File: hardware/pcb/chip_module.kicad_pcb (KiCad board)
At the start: 4 copper layers, 70 x 50 mm, 17 parts, among them J1 Samtec LSHM-130, U1 ADG732BCPZ, U2 ADG732BCPZ, U3 ADA4530-1, U4 74LVC1G04, U5 QSSC_Chip

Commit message: pcb: chip module copper-plane foundation + power-rail test points
route_qssc_pcb.py is board-agnostic (QSSC_PCB_PATH env override), so run the
copper-plane pass on the swappable chip module: 4 zones (In1.Cu GND, In2.Cu
+3V3, F.Cu/B.Cu GND floods) + 30 GND stitching vias -> the 64 analog detector
lines and the TIA sit over a continuous ground reference.

The +3V3 pour was an isolated-copper fill (all +3V3 pads are SMD, no plated
hole ties the In2.Cu plane to the rail). Each module PWR_FLAG now carries a
real thru-hole TestPoint_Loop footprint, giving 4 probeable power-rail points
(+3V3/+5V/+7V_EMIT/GND) on the left edge; the plated +3V3 pad stitches the
plane (same mechanism by which the main board's thru-hole RESET button keeps
its +3V3 plane non-isolated).

kicad-cli pcb drc: 0 violations / 0 unconnected / 0 footprint errors (was 1
isolated_copper warning). ERC unchanged (0 errors / 26 warnings). pytest 122
passed, 2 skipped; ruff clean.

Note recorded in HARDWARE_DESIGN.md §15A: TPS61023 (max output 5.5V) cannot
produce the +7V_EMIT rail — use a >=7V part (e.g. TPS61040) once the emitter
driver topology is fixed. *.kicad_prl gitignored (KiCad project-local file).

Co-Authored-By: Claude <noreply@anthropic.com>
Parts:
- added #FLG1: PWR_FLAG, TestPoint_Loop_D1.80mm_Drill1.0mm_Beaded, F.Cu at (6.00, 4.00)
- added #FLG2: PWR_FLAG, TestPoint_Loop_D1.80mm_Drill1.0mm_Beaded, F.Cu at (6.00, 9.00)
- added #FLG3: PWR_FLAG, TestPoint_Loop_D1.80mm_Drill1.0mm_Beaded, F.Cu at (6.00, 14.0)
- added #FLG4: PWR_FLAG, TestPoint_Loop_D1.80mm_Drill1.0mm_Beaded, F.Cu at (6.00, 19.0)
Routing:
- net GND: vias 0 -> 30
- added copper zone on In2.Cu, net +3V3
- added copper zone on B.Cu, net GND
- added copper zone on F.Cu, net GND
- added copper zone on In1.Cu, net GND

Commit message: chip module: place discrete MOSFET emitter crossbar (+5V), eliminate +7V_EMIT
Emitter driver for the 8x8 CQD matrix is now placed on the swappable chip
module as the simplest-functional topology (29 parts, no boost / no DAC /
no TLC5955): 2x 74HCT240 inverting level-shifters (3.3V FPGA -> 0/5V gate
drive, HCT TTL thresholds) + 8x AO3401A P-MOS high-side row switches +
8x AO3400A N-MOS low-side column sinks + 8x 220R set resistors + 3
decoupling. One pixel at a time, ~9mA at 2.2V headroom, matching
emitter_array.v (rows active-HIGH / cols active-LOW one-hot, idle all OFF).

Chip ER/EC pads rewired through the driver (ER{i}->emitter_anode{i},
EC{i}->emitter_cathode{i}); J1 still carries emitter_rows/cols -> 74HCT240
inputs. +7V_EMIT rail fully deleted on both boards: J1/J11 pin 59 -> GND
(extra pulsed-current return; connectors stay pin-for-pin mated), module
POWER_PINS/POWER_NETS/C6/#FLG3 removed. TIA is photovoltaic / zero-bias
(no MCP4921 DAC; DET_BIAS is a reserved spare). Module widened 70->85x50mm.

Verified headless: module ERC 0 errors / 53 warnings; module DRC 0
violations; main board ERC 0 errors / 139 warnings, DRC 0 violations.
pytest 122 passed / 2 skipped; ruff CI-gate clean. HARDWARE_DESIGN.md
\S1B/\S2/\S3/\S7/\S8/\S11/\S12/\S13/\S15A updated. RTL/XDC/sim/synth
untouched; new ~24 nets not yet routed (deferred GUI batch).

Co-Authored-By: Claude <noreply@anthropic.com>
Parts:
- removed #FLG3: PWR_FLAG, TestPoint_Loop_D1.80mm_Drill1.0mm_Beaded
- removed C6: 100nF, C_0603_1608Metric
- added C10: 10uF, C_0805_2012Metric, F.Cu at (62.0, 15.0)
- added C8: 100nF, C_0603_1608Metric, F.Cu at (62.0, 8.00)
- added C9: 100nF, C_0603_1608Metric, F.Cu at (62.0, 22.0)
- added Q1: AO3401A, SOT-23_Handsoldering, F.Cu at (64.0, 30.0)
- added Q10: AO3400A, SOT-23_Handsoldering, F.Cu at (82.0, 30.0)
- added Q11: AO3400A, SOT-23_Handsoldering, F.Cu at (76.0, 35.0)
- added Q12: AO3400A, SOT-23_Handsoldering, F.Cu at (82.0, 35.0)
- added Q13: AO3400A, SOT-23_Handsoldering, F.Cu at (76.0, 40.0)
- added Q14: AO3400A, SOT-23_Handsoldering, F.Cu at (82.0, 40.0)
- added Q15: AO3400A, SOT-23_Handsoldering, F.Cu at (76.0, 45.0)
- added Q16: AO3400A, SOT-23_Handsoldering, F.Cu at (82.0, 45.0)
- added Q2: AO3401A, SOT-23_Handsoldering, F.Cu at (70.0, 30.0)
- added Q3: AO3401A, SOT-23_Handsoldering, F.Cu at (64.0, 35.0)
- added Q4: AO3401A, SOT-23_Handsoldering, F.Cu at (70.0, 35.0)
- added Q5: AO3401A, SOT-23_Handsoldering, F.Cu at (64.0, 40.0)
- added Q6: AO3401A, SOT-23_Handsoldering, F.Cu at (70.0, 40.0)
- added Q7: AO3401A, SOT-23_Handsoldering, F.Cu at (64.0, 45.0)
- added Q8: AO3401A, SOT-23_Handsoldering, F.Cu at (70.0, 45.0)
- added Q9: AO3400A, SOT-23_Handsoldering, F.Cu at (76.0, 30.0)
- added R1: 220R, R_0603_1608Metric, F.Cu at (72.0, 13.0)
- added R2: 220R, R_0603_1608Metric, F.Cu at (75.0, 13.0)
- added R3: 220R, R_0603_1608Metric, F.Cu at (78.0, 13.0)
- added R4: 220R, R_0603_1608Metric, F.Cu at (81.0, 13.0)
- added R5: 220R, R_0603_1608Metric, F.Cu at (72.0, 16.0)
- added R6: 220R, R_0603_1608Metric, F.Cu at (75.0, 16.0)
- added R7: 220R, R_0603_1608Metric, F.Cu at (78.0, 16.0)
- added R8: 220R, R_0603_1608Metric, F.Cu at (81.0, 16.0)
- added U6: 74HCT240, TSSOP-20_4.4x6.5mm_P0.65mm, F.Cu at (68.0, 8.00)
- added U7: 74HCT240, TSSOP-20_4.4x6.5mm_P0.65mm, F.Cu at (68.0, 22.0)
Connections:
- J1 pad 59: +7V_EMIT -> GND
- U5 pad EC0: emitter_cols0 -> emitter_cathode0
- U5 pad EC1: emitter_cols1 -> emitter_cathode1
- U5 pad EC2: emitter_cols2 -> emitter_cathode2
- U5 pad EC3: emitter_cols3 -> emitter_cathode3
- U5 pad EC4: emitter_cols4 -> emitter_cathode4
- U5 pad EC5: emitter_cols5 -> emitter_cathode5
- U5 pad EC6: emitter_cols6 -> emitter_cathode6
- U5 pad EC7: emitter_cols7 -> emitter_cathode7
- U5 pad ER0: emitter_rows0 -> emitter_anode0
- U5 pad ER1: emitter_rows1 -> emitter_anode1
- U5 pad ER2: emitter_rows2 -> emitter_anode2
- U5 pad ER3: emitter_rows3 -> emitter_anode3
- U5 pad ER4: emitter_rows4 -> emitter_anode4
- U5 pad ER5: emitter_rows5 -> emitter_anode5
- U5 pad ER6: emitter_rows6 -> emitter_anode6
- U5 pad ER7: emitter_rows7 -> emitter_anode7
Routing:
- net GND: vias 30 -> 0
- removed copper zone on In2.Cu, net +3V3
- removed copper zone on B.Cu, net GND
- removed copper zone on F.Cu, net GND
- removed copper zone on In1.Cu, net GND
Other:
- board size 70 x 50 mm -> 85 x 50 mm

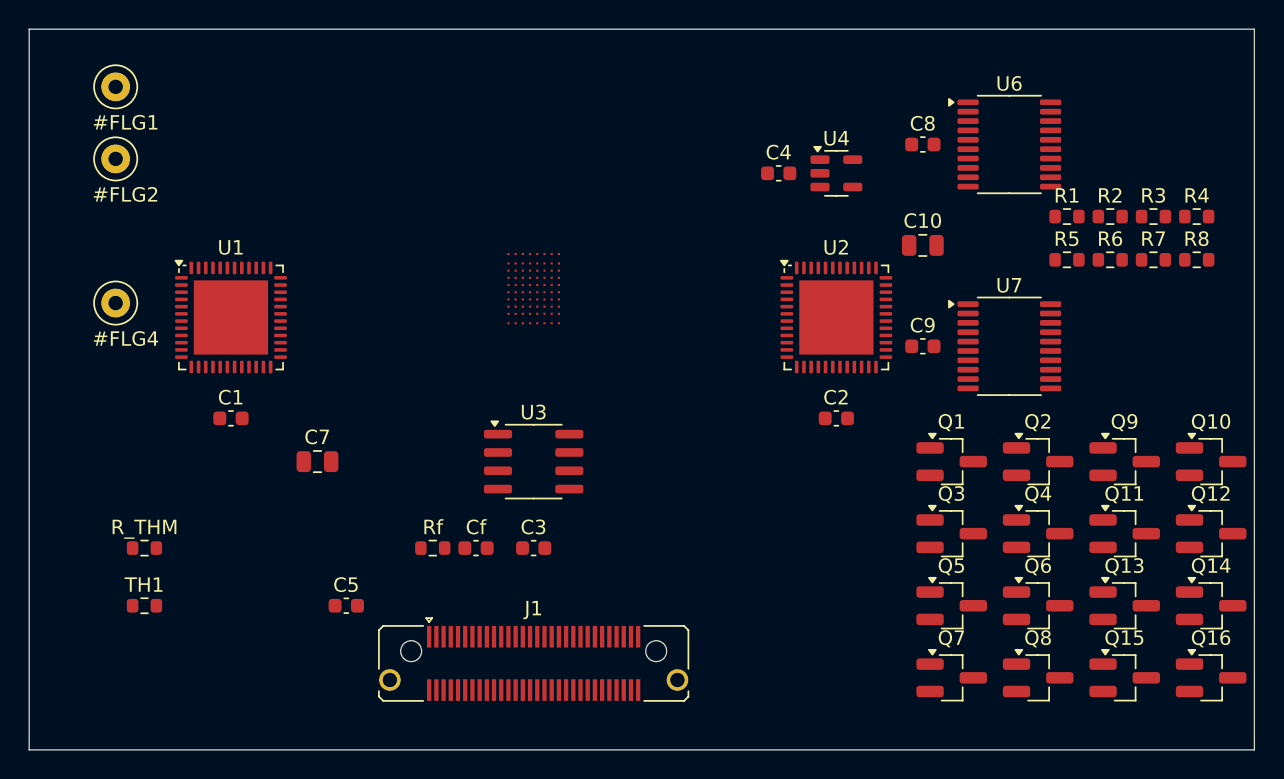
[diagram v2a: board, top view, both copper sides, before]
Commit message: pcb: route both boards headlessly (1st-pass signals + planes), DRC 0/0/0
Run the headless routing pipeline on BOTH boards and commit the routed copper.

Main board (route_signals.py then route_qssc_pcb.py):
- 16 BGA via-in-pad fanouts (0.20/0.10mm HDI-lite)
- first-pass line routing of 19/71 signal nets (118 segments, 28 routing vias)
- 4 zones (In1.Cu GND plane, In2.Cu +3V3 plane, F.Cu+B.Cu GND floods)
- 99 GND stitching vias  -> 143 vias total

Chip module (route_signals.py + route_qssc_pcb.py):
- BGA fanout SKIPPED via a new pad-count guard (U1 is an ADG732 QFN-48,
  not a BGA -- via-in-pad on a QFN pad is a fabrication defect)
- first-pass line routing of 14 nets (54 segments, 15 routing vias)
- 4 zones + 33 GND stitching vias  -> 48 vias total

Both boards: kicad-cli pcb drc -> 0 violations / 0 unconnected / 0 fp errors.

route_signals.py fixes:
- vip_vias was dict[net->via] overwriting -> multi-ball nets leaked vias;
  now dict[net->list[via]] via setdefault().append()
- via-in-pad removal: condition changed from `net not in done_set` (wrongly
  removed +3V3 plane vias) to `net in fail_set`; plane nets (GND/+3V3) KEEP
  their through-hole vias so they reach In1.Cu GND / In2.Cu +3V3 on 2 layers

gen_qssc_kicad.py (shared emit_pro): add via_dangling/track_dangling=ignore
-- same incompleteness class as unconnected_items=ignore on a partially-routed
design-artifact board; real electrical errors (shorts/clearance/courtyard)
are still caught.

Test fixes (the verification gate):
- test_pcb_route.py: hardcoded GND netcode "13" broke after board regen
  shifted GND to netcode 16; now resolves GND's netcode dynamically from the
  (net N "GND") declaration and asserts that netcode is in via_nets
- test_pcb_route_signals.py: "+3V3 not in via_nets" was a genuine test bug --
  GND balls connect via the F.Cu GND flood (no via -> correctly skipped) but
  +3V3 balls have no F.Cu +3V3 pour (plane is In2.Cu only) so they NEED the
  through-hole via-in-pad to reach their plane;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
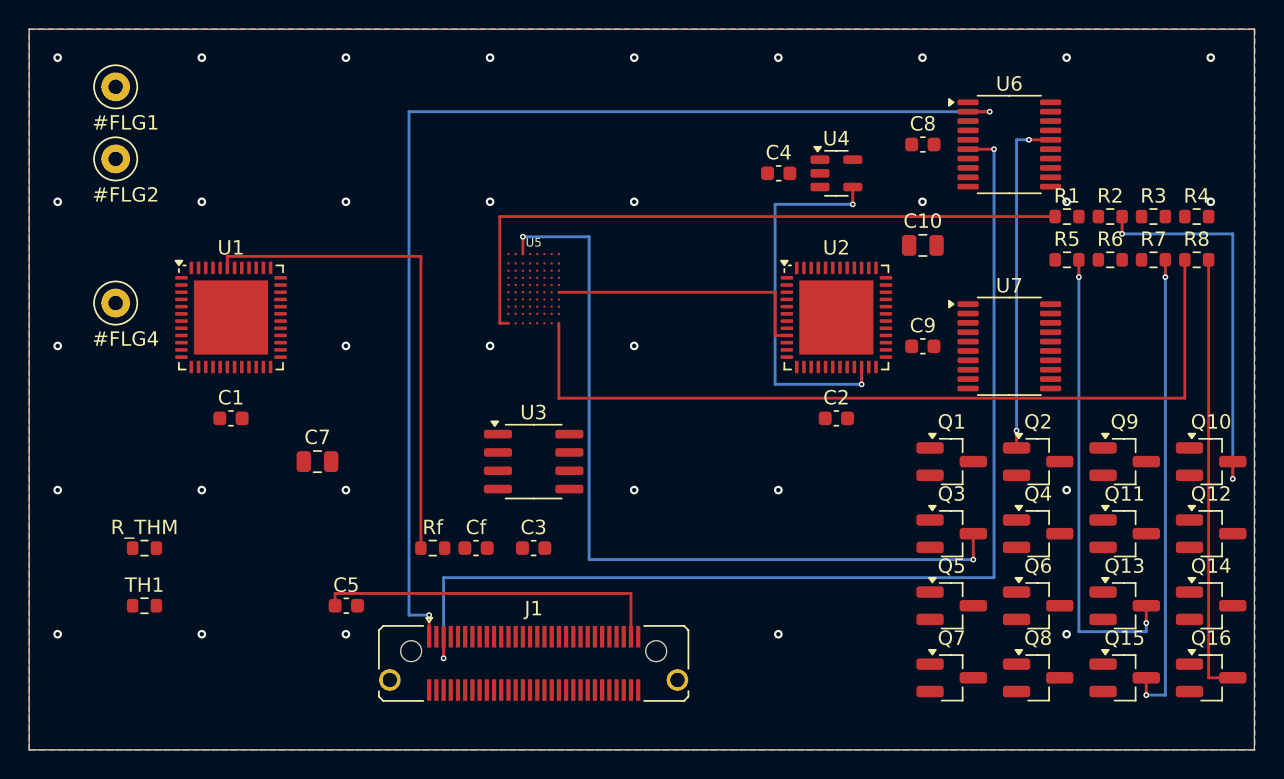
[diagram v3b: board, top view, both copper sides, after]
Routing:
- net emitter_rows0: track 0.00 -> 79.6 mm, vias 0 -> 2
- net emitter_rows2: track 0.00 -> 76.8 mm, vias 0 -> 2
- net emitter_cathode7: track 0.00 -> 58.2 mm
- net emitter_anode2: track 0.00 -> 56.6 mm, vias 0 -> 2
- net emitter_cathode0: track 0.00 -> 46.5 mm
- net TIA_IN: track 0.00 -> 34.5 mm
- net col_sink6: track 0.00 -> 32.7 mm, vias 0 -> 2
- net col_sink4: track 0.00 -> 32.3 mm, vias 0 -> 2
- net col_sink7: track 0.00 -> 30.7 mm
- net col_sink1: track 0.00 -> 27.1 mm, vias 0 -> 2
- net MUX_EN2: track 0.00 -> 26.3 mm, vias 0 -> 2
- net +5V: track 0.00 -> 24.4 mm
- net row_gate1: track 0.00 -> 23.7 mm, vias 0 -> 2
- net DET_IN39: track 0.00 -> 18.8 mm
- net GND: vias 0 -> 32
- added copper zone on In2.Cu, net +3V3
- added copper zone on B.Cu, net GND
- added copper zone on F.Cu, net GND
- added copper zone on In1.Cu, net GND
